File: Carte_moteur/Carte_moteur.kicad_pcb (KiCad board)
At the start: 2 copper layers, 117 parts, among them J101 Conn_01x02_Socket, J102 Conn_01x02, J103 Conn_01x02, J104 Conn_01x07, J201 Conn_01x05_Pin, J202 Conn_01x04_Pin, J301 Conn_01x05_Pin, J302 Conn_01x04_Pin, J401 Conn_01x05_Pin, J402 Conn_01x04_Pin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

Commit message: updated motor PCB
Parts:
- removed C501, C507: C, Capacitor_SMD:C_0603_1608Metric_Pad1.08x0.95mm_HandSolder
- removed C502: C, Capacitor_SMD:C_0805_2012Metric_Pad1.18x1.45mm_HandSolder
- removed R205, R305, R405, R501, R502, R503, R504, R505, R506, R507, R508, R509: R_US, Resistor_SMD:R_0603_1608Metric_Pad0.98x0.95mm_HandSolder
- removed SW201, SW301, SW401: SW_DIP_x02, Button_Switch_THT:SW_DIP_SPSTx02_Slide_9.78x7.26mm_W7.62mm_P2.54mm
- added C508: C, Capacitor_SMD:C_0603_1608Metric_Pad1.08x0.95mm_HandSolder, B.Cu at (103.9, 106.4)
- added H101: MountingHole_Pad, MountingHole:MountingHole_3.2mm_M3_DIN965_Pad, F.Cu at (79.5, 97.0)
- added H102: MountingHole_Pad, MountingHole:MountingHole_3.2mm_M3_DIN965_Pad, F.Cu at (144.8, 97.0)
- added H103: MountingHole_Pad, MountingHole:MountingHole_3.2mm_M3_DIN965_Pad, F.Cu at (80.0, 163.6)
- added H104: MountingHole_Pad, MountingHole:MountingHole_3.2mm_M3_DIN965_Pad, F.Cu at (145.0, 163.6)
- added J105: Conn_01x02_Socket, Connector_Molex:Molex_KK-396_A-41791-0002_1x02_P3.96mm_Vertical, F.Cu at (83.3, 123.7)
- added J106: Conn_01x07, Connector_Molex:Molex_KK-254_AE-6410-07A_1x07_P2.54mm_Vertical, F.Cu at (89.2, 101.6)
- added R210: R_US, Resistor_SMD:R_0603_1608Metric_Pad0.98x0.95mm_HandSolder, B.Cu at (94.8, 130.8)
- added R211: R_US, Resistor_SMD:R_0603_1608Metric_Pad0.98x0.95mm_HandSolder, B.Cu at (97.3, 130.8)
- added R212: R_US, Resistor_SMD:R_0603_1608Metric_Pad0.98x0.95mm_HandSolder, B.Cu at (99.8, 130.8)
- added R523: R_US, Resistor_SMD:R_0603_1608Metric_Pad0.98x0.95mm_HandSolder, B.Cu at (114.1, 130.8)
- added R524: R_US, Resistor_SMD:R_0603_1608Metric_Pad0.98x0.95mm_HandSolder, B.Cu at (116.6, 130.8)
- added R525: R_US, Resistor_SMD:R_0603_1608Metric_Pad0.98x0.95mm_HandSolder, B.Cu at (119.1, 130.8)
- added R526: R_US, Resistor_SMD:R_0603_1608Metric_Pad0.98x0.95mm_HandSolder, B.Cu at (133.4, 130.8)
- added R527: R_US, Resistor_SMD:R_0603_1608Metric_Pad0.98x0.95mm_HandSolder, B.Cu at (135.9, 130.8)
- added R528: R_US, Resistor_SMD:R_0603_1608Metric_Pad0.98x0.95mm_HandSolder, B.Cu at (138.4, 130.8)
- C101, C102, C104, C503, C504, C505, C506, C602, C605, Q601, R101, R102, R103, R104, R105, R510, R511, R603, R604, R605, R606, R609, R612: moved to B.Cu
- moved R104 491.5 mm to (130.2, 114.2), turned to 90 degrees
- moved R105 488.4 mm to (127.6, 114.3), turned to 90 degrees
- moved R102 487.9 mm to (125.1, 114.2), turned to 90 degrees
- moved R103 484.8 mm to (122.6, 114.2), turned to 90 degrees
- moved R101 483.2 mm to (119.9, 112.8), turned to 90 degrees
- moved J104 481.0 mm to (114.9, 117.0)
- moved R615 477.2 mm to (143.0, 117.6)
- moved R616 477.0 mm to (143.1, 112.0)
- moved D604 473.4 mm to (143.4, 113.8), turned to 180 degrees
- moved D603 473.3 mm to (143.4, 115.8), turned to 0 degrees
- moved D601 471.9 mm to (138.5, 112.0), turned to 0 degrees
- moved U602 471.6 mm to (136.5, 116.8)
- moved C602 468.7 mm to (136.5, 117.8), turned to -90 degrees
- moved J602 465.7 mm to (144.5, 105.7), turned to 90 degrees
- moved D602 464.5 mm to (138.4, 109.5), turned to 0 degrees
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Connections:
- J104 pad 4: /micro/T_SWCLK -> /micro/T_SWDIO
- J104 pad 5: /micro/T_SWDIO -> /micro/T_SWCLK
- J104 pad 6: /micro/T_SWO -> /micro/T_JDTI
- J104 pad 7: /micro/T_JDTI -> /micro/T_SWO
- J201 pad 2: /micro/TIM1_CH1 -> /micro/TIM5_CH1
- J201 pad 3: /micro/TIM1_CH2 -> /micro/TIM5_CH2
- J201 pad 4: /micro/TIM1_ETR -> /micro/TIM5_ETR
- J301 pad 2: /micro/TIM3_CH1 -> /micro/TIM1_CH1
- J301 pad 3: /micro/TIM3_CH2 -> /micro/TIM1_CH2
- J301 pad 4: /micro/TIM3_ETR -> /micro/TIM1_ETR
- J401 pad 2: /micro/TIM5_CH1 -> /micro/TIM3_CH1
- J401 pad 3: /micro/TIM5_CH2 -> /micro/TIM3_CH2
- J401 pad 4: /micro/TIM5_ETR -> /micro/TIM3_ETR
- R512 pad 1: /micro/TMC1 -> /micro/TMC2
- R513 pad 1: /micro/TMC1 -> /micro/TMC2
- R514 pad 1: /micro/TMC3 -> /micro/TMC1
- R515 pad 1: /micro/TMC3 -> /micro/TMC1
- R516 pad 1: /micro/TMC2 -> /micro/TMC3
- R517 pad 1: /micro/TMC2 -> /micro/TMC3
- U201 pad 4: Net-(R205-Pad2) -> /micro/TMC1
- U201 pad 7: /micro/HRTIM_CHA1 -> /micro/HRTIM_CHE1
- U201 pad 8: /micro/HRTIM_CHA2 -> /micro/HRTIM_CHE2
- U301 pad 4: Net-(R305-Pad2) -> /micro/TMC2
- U301 pad 7: /micro/HRTIM_CHB1 -> /micro/HRTIM_CHD1
- U301 pad 8: /micro/HRTIM_CHB2 -> /micro/HRTIM_CHD2
- U401 pad 4: Net-(R405-Pad2) -> /micro/TMC3
- U401 pad 7: /micro/HRTIM_CHE1 -> /micro/HRTIM_CHB1
- U401 pad 8: /micro/HRTIM_CHE2 -> /micro/HRTIM_CHB2
- U501 pad 30: /micro/UART3_TX -> unconnected-(U501-PB10-Pad30)
- U501 pad 36: unconnected-(U501-PB14-Pad36) -> /micro/HRTIM_CHD1
- U501 pad 37: unconnected-(U501-PB15-Pad37) -> /micro/HRTIM_CHD2
- U501 pad 42: /micro/HRTIM_CHA1 -> unconnected-(U501-PA8-Pad42)
- U501 pad 43: /micro/HRTIM_CHA2 -> unconnected-(U501-PA9-Pad43)
- U501 pad 62: unconnected-(U501-PB9-Pad62) -> /micro/UART3_TX
- U603 pad 12: /micro/LPUART1_RX -> /micro/UART4_RX
- U603 pad 13: /micro/LPUART1_TX -> /micro/UART4_TX
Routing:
- net GND: track 122.3 -> 1265.6 mm, vias 8 -> 68
- net +3V3: track 8.65 -> 209.4 mm, vias 0 -> 7
- net +5V: track 0.00 -> 125.6 mm, vias 0 -> 1
- net +BATT: track 11.8 -> 117.8 mm
- net /micro/TMC3: track 0.00 -> 89.5 mm, vias 0 -> 2
- net /micro/TMC2: track 0.00 -> 78.3 mm, vias 0 -> 2
- net /micro/TMC1: track 0.00 -> 61.2 mm, vias 0 -> 2
- net /micro/TIM3_CH2: track 0.00 -> 61.1 mm, vias 0 -> 2
- net /micro/HRTIM_CHB1: track 0.00 -> 51.6 mm
- net /micro/HRTIM_CHB2: track 0.00 -> 47.6 mm
- net /micro/TIM3_CH1: track 0.00 -> 44.5 mm, vias 0 -> 2
- net /micro/TIM3_ETR: track 0.00 -> 42.4 mm, vias 0 -> 2
- net /micro/TIM5_CH1: track 0.00 -> 42.4 mm, vias 0 -> 1
- net /micro/TIM1_CH2: track 0.00 -> 42.1 mm, vias 0 -> 1
- net /micro/HRTIM_CHD1: track 0.00 -> 40.7 mm, vias 0 -> 2
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- added copper zone on B.Cu, net GND
- added copper zone on F.Cu, net GND
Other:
- board outline added: 72.6 x 73.7 mm
- board text added: "+5V"
- board text added: "BATT"
- board text added: "COM"

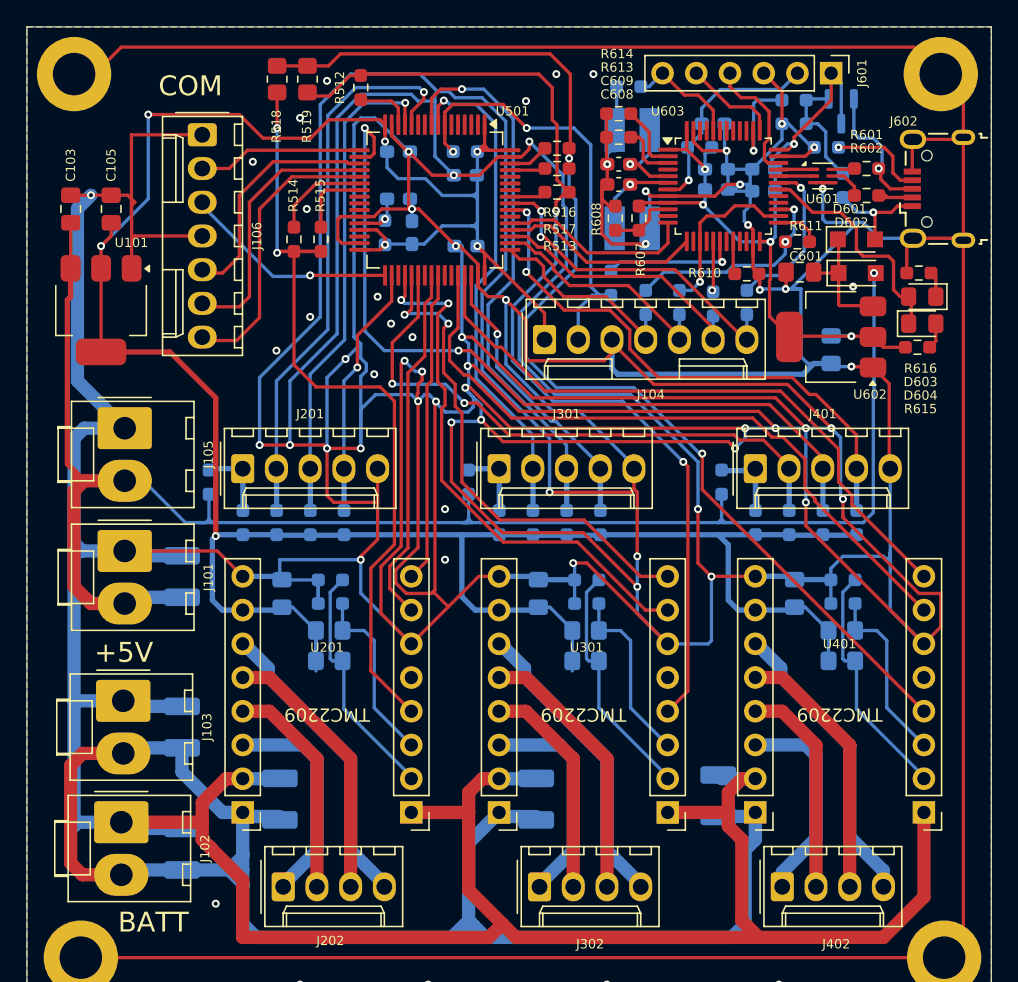
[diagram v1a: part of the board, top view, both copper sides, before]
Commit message: debug led added. Modified power connector
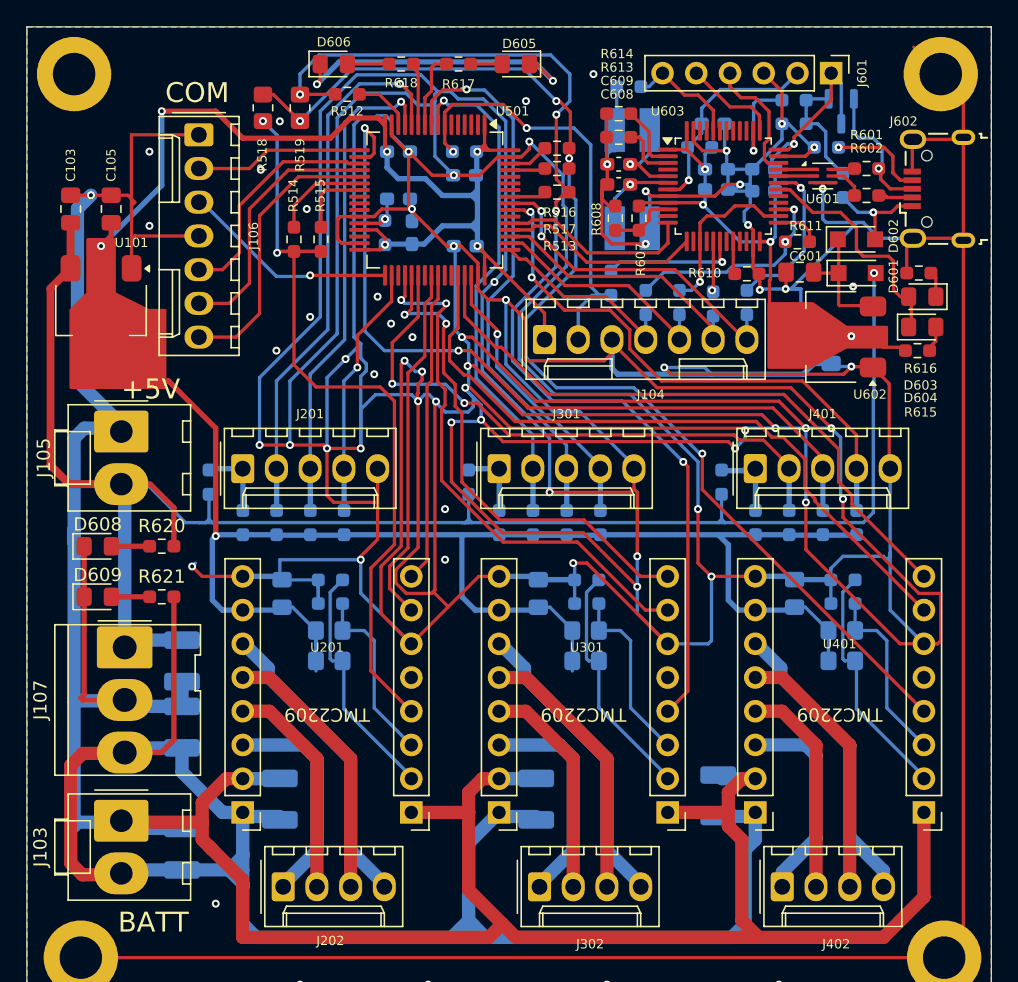
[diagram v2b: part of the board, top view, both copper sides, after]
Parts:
- removed J101: Conn_01x02_Socket, Connector_Molex:Molex_KK-396_A-41791-0002_1x02_P3.96mm_Vertical
- removed J102: Conn_01x02, Connector_Molex:Molex_KK-396_A-41791-0002_1x02_P3.96mm_Vertical
- added D605: LED, LED_SMD:LED_0805_2012Metric_Pad1.15x1.40mm_HandSolder, F.Cu at (112.8, 96.3)
- added D606: LED, LED_SMD:LED_0805_2012Metric_Pad1.15x1.40mm_HandSolder, F.Cu at (99.1, 96.3)
- added D608: LED, LED_SMD:LED_0805_2012Metric_Pad1.15x1.40mm_HandSolder, F.Cu at (81.3, 132.6)
- added D609: LED, LED_SMD:LED_0805_2012Metric_Pad1.15x1.40mm_HandSolder, F.Cu at (81.3, 136.4)
- added J107: Conn_01x03, Connector_Molex:Molex_KK-396_5273-03A_1x03_P3.96mm_Vertical, F.Cu at (83.3, 140.2)
- added R617: R_US, Resistor_SMD:R_0603_1608Metric_Pad0.98x0.95mm_HandSolder, F.Cu at (108.5, 96.3)
- added R618: R_US, Resistor_SMD:R_0603_1608Metric_Pad0.98x0.95mm_HandSolder, F.Cu at (104.1, 96.3)
- added R620: R_US, Resistor_SMD:R_0603_1608Metric_Pad0.98x0.95mm_HandSolder, F.Cu at (86.1, 132.6)
- added R621: R_US, Resistor_SMD:R_0603_1608Metric_Pad0.98x0.95mm_HandSolder, F.Cu at (86.1, 136.4)
- J105: value Conn_01x02_Socket -> Conn_01x02
- moved J103 9.03 mm to (83.1, 153.3)
- moved C101 6.35 mm to (87.6, 141.2), turned to -90 degrees
- moved R518 2.41 mm to (93.7, 99.6)
- moved R519 2.23 mm to (96.5, 99.6), turned to 90 degrees
- moved R512 1.14 mm to (100.1, 98.6), turned to 0 degrees
- moved J105 0.36 mm to (83.1, 124.0)
- moved D603 0.25 mm to (143.4, 116.1)
- moved J106 0.25 mm to (88.9, 101.6)
- moved R615 0.25 mm to (143.0, 117.9)
- moved C505 0.06 mm to (109.0, 110.0)
- moved C503 0.06 mm to (108.9, 104.6)
- moved R510 0.06 mm to (108.9, 102.9)
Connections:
- U501 pad 10: unconnected-(U501-PC2-Pad10) -> Net-(U501-PC2)
- U501 pad 11: unconnected-(U501-PC3-Pad11) -> Net-(U501-PC3)
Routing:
- net GND: track 1265.6 -> 1248.7 mm, vias 68 -> 73
- net +BATT: track 117.8 -> 132.7 mm
- net /micro/TMC2: track 78.3 -> 85.2 mm, vias 2 -> 4
- net +5V: track 125.6 -> 131.9 mm
- net Net-(U501-PC2): track 0.00 -> 5.75 mm
- net +3V3: track 209.4 -> 214.8 mm
- net Net-(U501-PC3): track 0.00 -> 4.42 mm
- net Net-(D606-A): track 0.00 -> 3.14 mm
- net Net-(D609-A): track 0.00 -> 2.89 mm
- net Net-(D608-A): track 0.00 -> 2.88 mm
- net Net-(D605-A): track 0.00 -> 2.38 mm
- net /micro/TMC1: track 61.2 -> 59.5 mm
- net /micro/TIM5_CH1: track 42.4 -> 41.2 mm
- net /micro/TMC3: track 89.5 -> 90.5 mm, vias 2 -> 4
- net /micro/TIM3_CH2: track 61.1 -> 60.3 mm
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
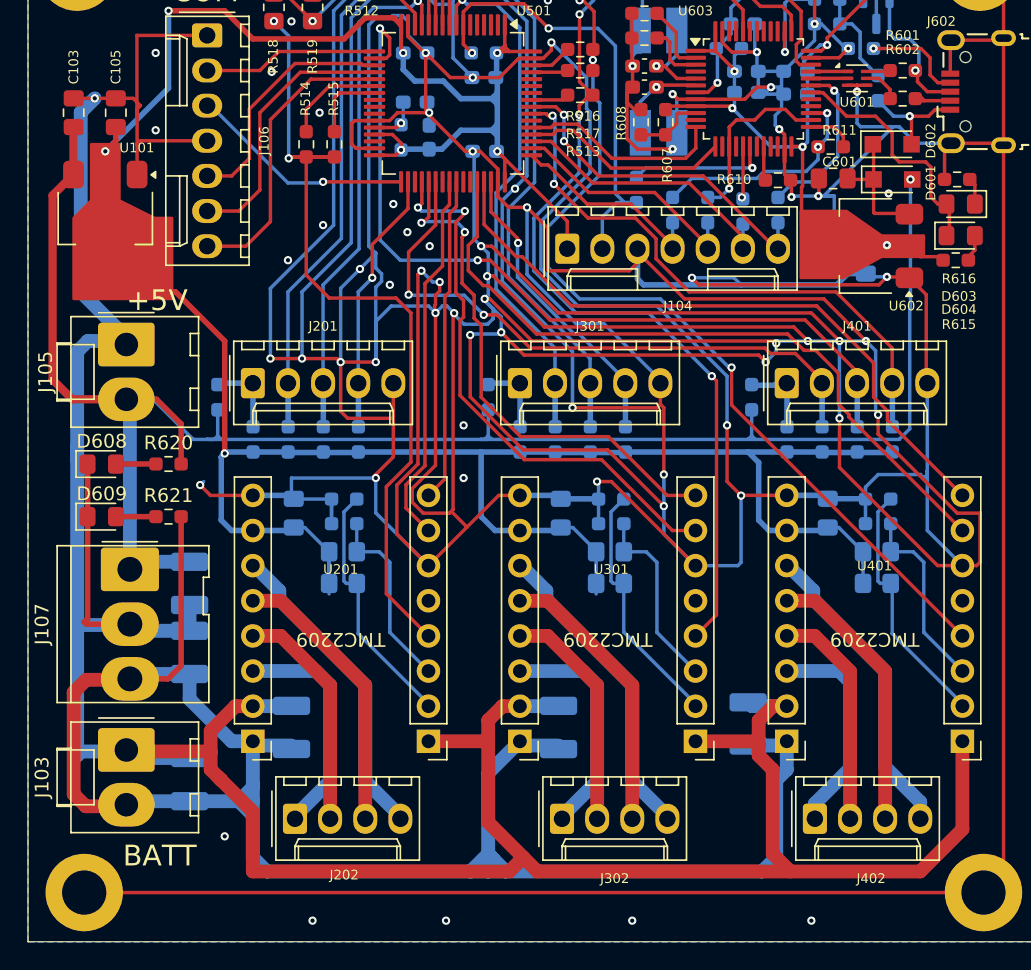
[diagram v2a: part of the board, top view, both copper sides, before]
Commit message: changed pwr connector
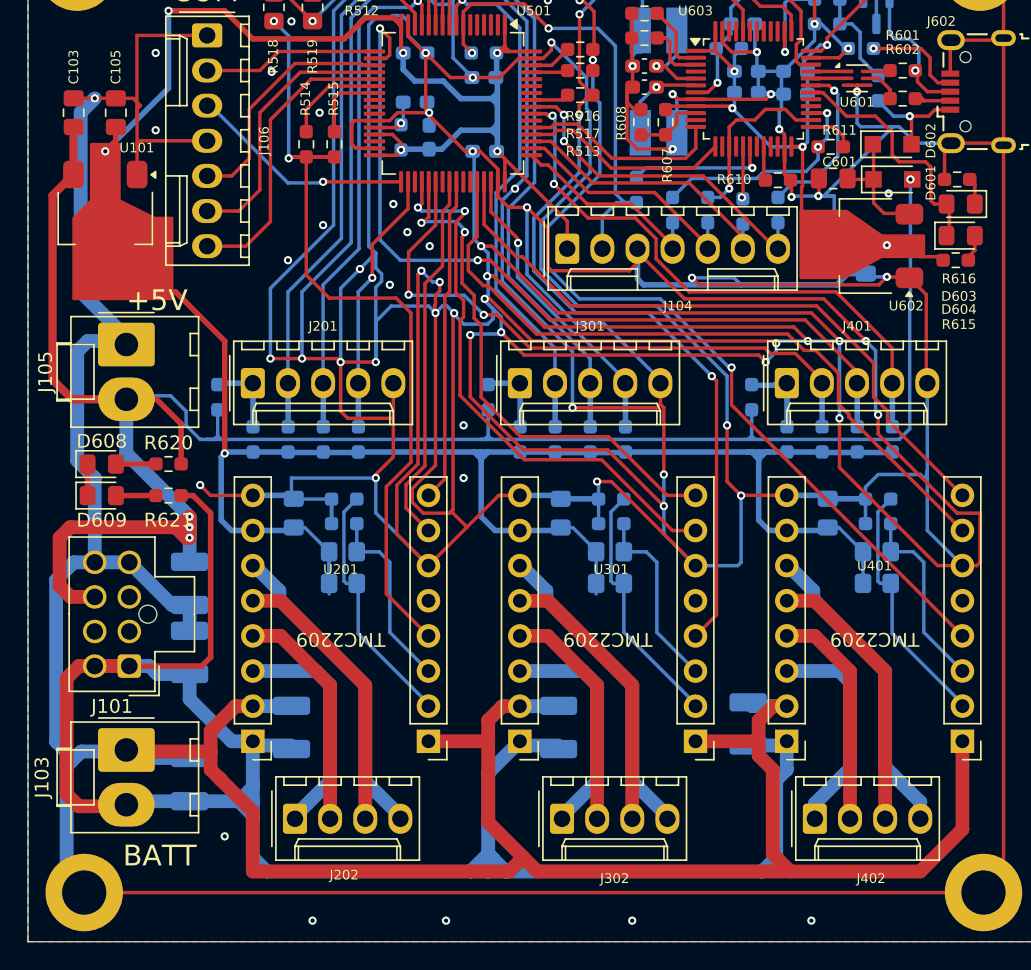
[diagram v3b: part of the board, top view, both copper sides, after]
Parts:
- removed J107: Conn_01x03, Connector_Molex:Molex_KK-396_5273-03A_1x03_P3.96mm_Vertical
- added J101: Conn_02x04_Top_Bottom, Connector_Molex:Molex_Nano-Fit_105310-xx08_2x04_P2.50mm_Vertical, F.Cu at (83.3, 147.2)
- moved D609 1.52 mm to (81.3, 134.9)
- moved R621 1.52 mm to (86.1, 134.9)
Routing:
- net +5V: track 131.9 -> 151.1 mm, vias 1 -> 4
- net +BATT: track 132.7 -> 142.2 mm
- net +3V3: track 214.8 -> 217.6 mm
